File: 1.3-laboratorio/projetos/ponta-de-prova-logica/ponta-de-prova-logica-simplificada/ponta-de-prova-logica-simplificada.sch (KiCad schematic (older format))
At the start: 18 parts, among them J1 TEST PROBE, J2 Conn_01x02, U1 LM319

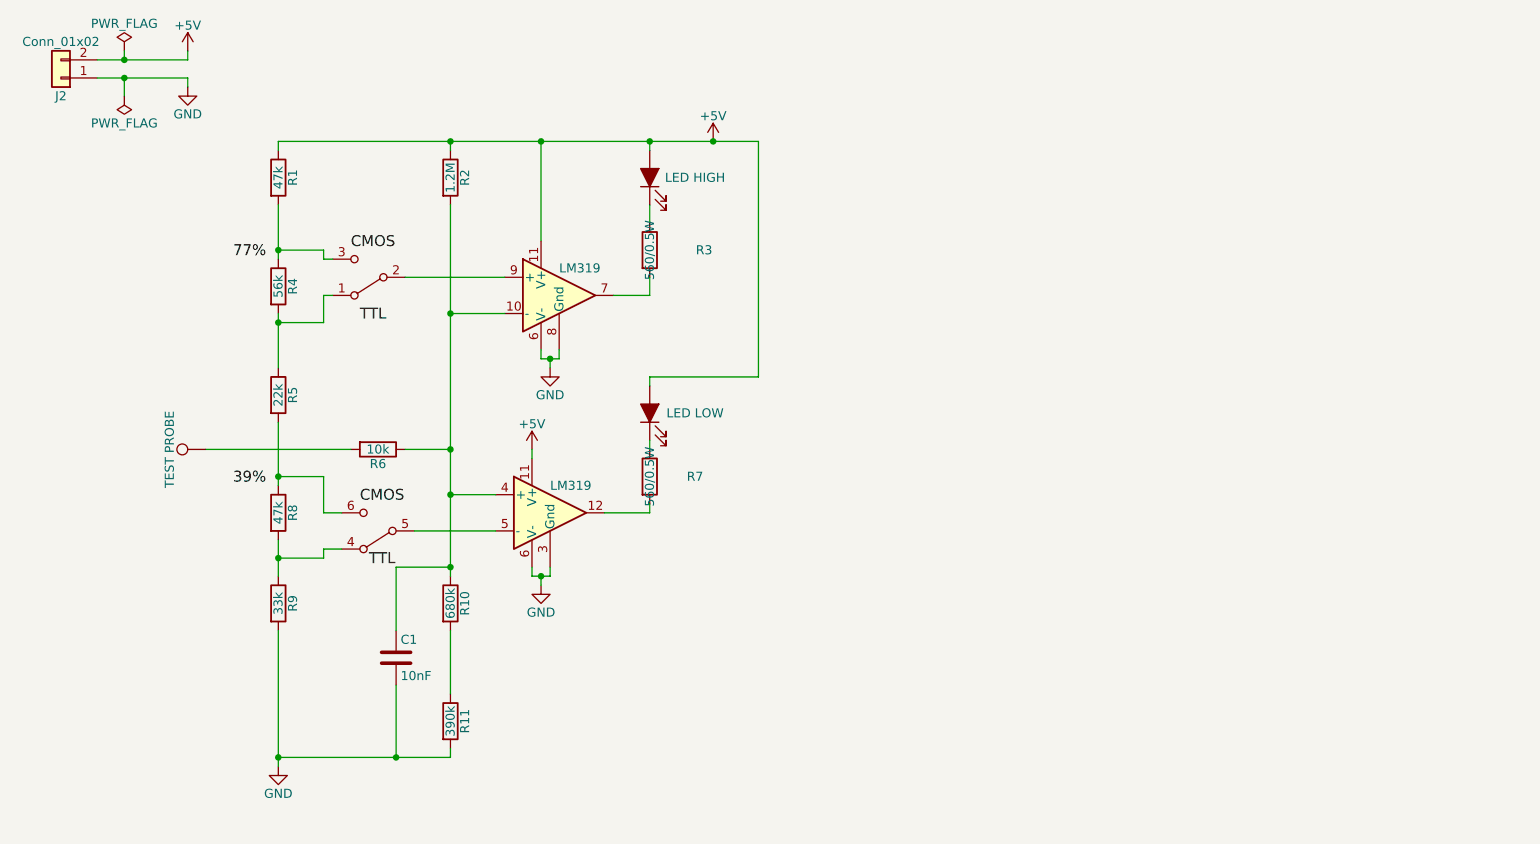
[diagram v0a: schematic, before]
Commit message: Nova versão da Ponta de Prova Lógica com o LM339.
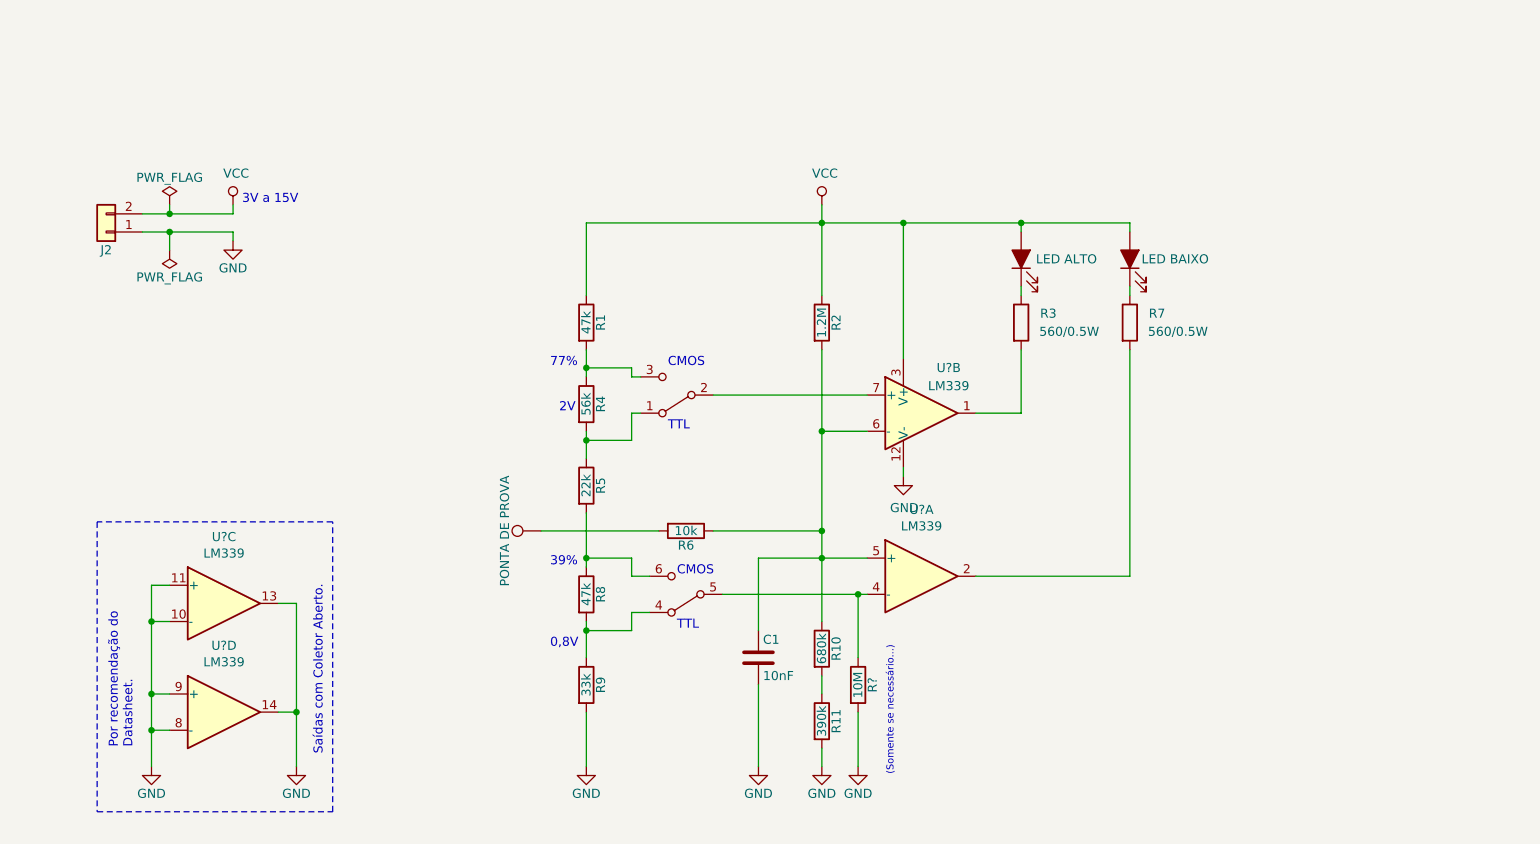
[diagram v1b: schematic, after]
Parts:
- removed U1: LM319, Housings_DIP:DIP-14_W7.62mm, symbol ponta-de-prova-logica-simplificada-rescue:LM319
- added R?: 10M, Resistors_THT:R_Axial_DIN0207_L6.3mm_D2.5mm_P7.62mm_Horizontal, symbol Device:R
- added U? (x5): LM339, symbol Comparator:LM339
- D1: value LED HIGH -> LED ALTO
- D2: value LED LOW -> LED BAIXO
- J1: value TEST PROBE -> PONTA DE PROVA
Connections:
- net GND: now also R?.2, U?.10 (-), U?.11 (+), U?.12 (V-), U?.13, U?.14, U?.8 (-), U?.9 (+)
- net at C1.1, R10.1, R2.2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: now also U?.5 (+), U?.6 (-)
- net at R3.2: now also U?.1
- net at TTL1.2 (B): now also U?.7 (+)
- net at R7.2: now also U?.2
- net at TTL1.5 (B): now also R?.1, U?.4 (-)
- net +5V renamed VCC
- net VCC: now also U?.3 (V+)
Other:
- note added: "(Somente se necessário...)"
- note added: "0,8V"
- note added: "2V"
- note added: "39%"
- note added: "3V a 15V"
- note added: "77%"
- note added: "CMOS"
- note added: "Por recomendação do\nDatasheet."
- note added: "Saídas com Coletor Aberto."
- note added: "TTL"
- moved on the sheet: C1, J2, R1, R10, R11, R2, R3, R4, R5, R6, R7, R8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

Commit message: Nova versão da Ponta de Prova Lógica - PCI em elaboração.
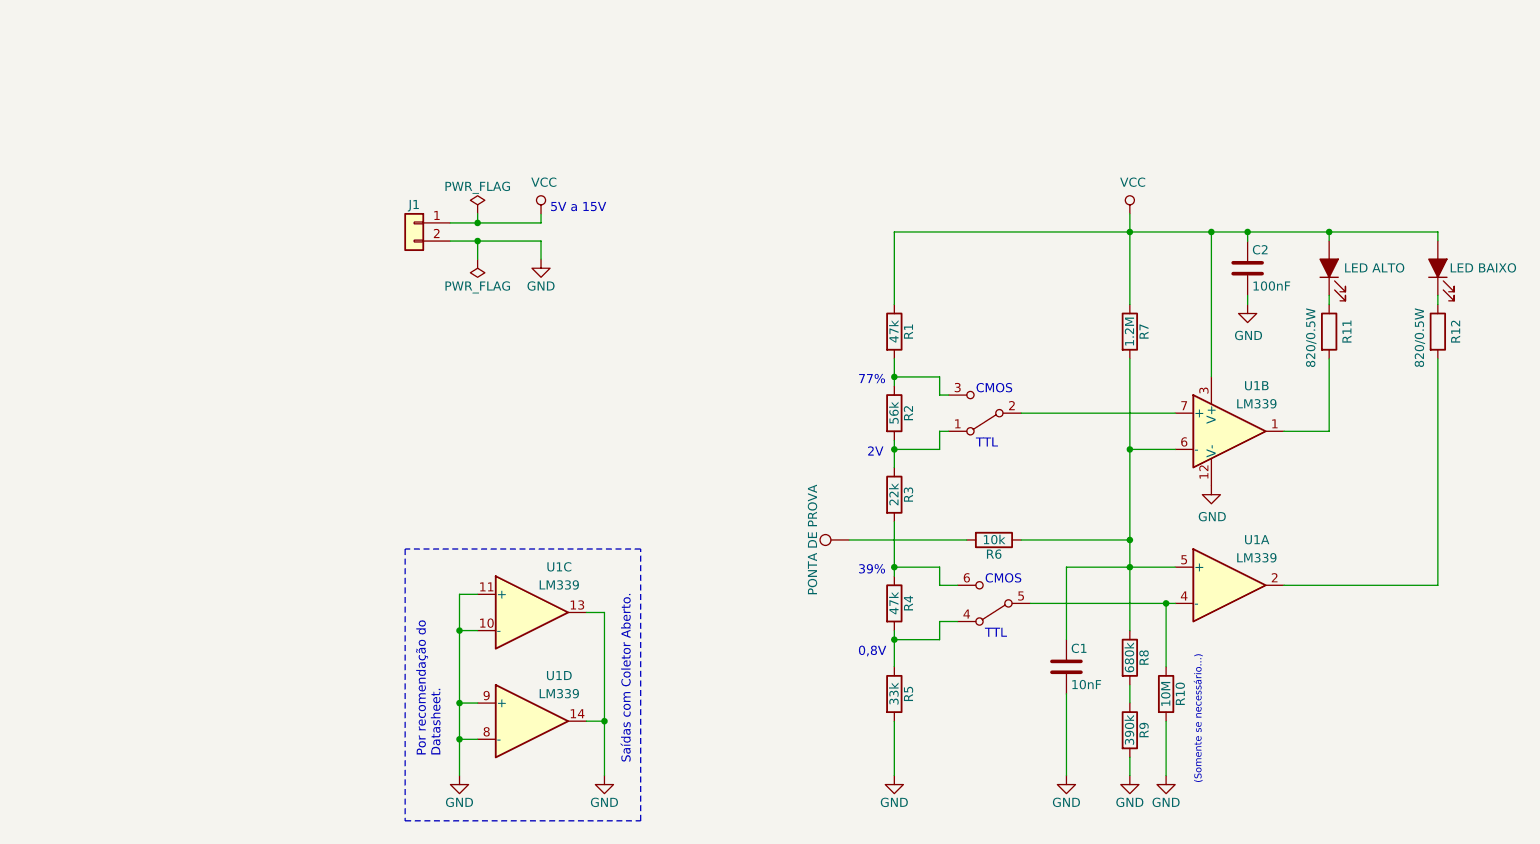
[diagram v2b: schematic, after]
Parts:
- added C2: 100nF, Capacitor_THT:C_Disc_D5.0mm_W2.5mm_P5.00mm, symbol Device:C
- C1: footprint Capacitors_THT:C_Disc_D5.0mm_W2.5mm_P5.00mm -> Capacitor_THT:C_Disc_D5.0mm_W2.5mm_P5.00mm
- D1, D2: footprint LEDs:LED_D4.0mm -> LED_THT:LED_D3.0mm
- J1: renamed from J2; footprint Connectors_Terminal_Blocks:TerminalBlock_Altech_AK300-2_P5.00mm -> TerminalBlock:TerminalBlock_Altech_AK300-2_P5.00mm
- J2: renamed from J1; footprint Connectors:Pin_d1.0mm_L10.0mm -> Connector_Wire:SolderWirePad_1x01_Drill0.8mm
- R1, R6: footprint Resistors_THT:R_Axial_DIN0207_L6.3mm_D2.5mm_P7.62mm_Horizontal -> Resistor_THT:R_Axial_DIN0207_L6.3mm_D2.5mm_P7.62mm_Horizontal
- R10: renamed from R?; footprint Resistors_THT:R_Axial_DIN0207_L6.3mm_D2.5mm_P7.62mm_Horizontal -> Resistor_THT:R_Axial_DIN0207_L6.3mm_D2.5mm_P7.62mm_Horizontal
- R11: renamed from R3; value 560/0.5W -> 820/0.5W; footprint Resistors_THT:R_Axial_DIN0207_L6.3mm_D2.5mm_P7.62mm_Horizontal -> Resistor_THT:R_Axial_DIN0207_L6.3mm_D2.5mm_P7.62mm_Horizontal
- R12: renamed from R7; value 560/0.5W -> 820/0.5W; footprint Resistors_THT:R_Axial_DIN0207_L6.3mm_D2.5mm_P7.62mm_Horizontal -> Resistor_THT:R_Axial_DIN0207_L6.3mm_D2.5mm_P7.62mm_Horizontal
- R2: renamed from R4; footprint Resistors_THT:R_Axial_DIN0207_L6.3mm_D2.5mm_P7.62mm_Horizontal -> Resistor_THT:R_Axial_DIN0207_L6.3mm_D2.5mm_P7.62mm_Horizontal
- R3: renamed from R5; footprint Resistors_THT:R_Axial_DIN0207_L6.3mm_D2.5mm_P7.62mm_Horizontal -> Resistor_THT:R_Axial_DIN0207_L6.3mm_D2.5mm_P7.62mm_Horizontal
- R4: renamed from R8; footprint Resistors_THT:R_Axial_DIN0207_L6.3mm_D2.5mm_P7.62mm_Horizontal -> Resistor_THT:R_Axial_DIN0207_L6.3mm_D2.5mm_P7.62mm_Horizontal
- R5: renamed from R9; footprint Resistors_THT:R_Axial_DIN0207_L6.3mm_D2.5mm_P7.62mm_Horizontal -> Resistor_THT:R_Axial_DIN0207_L6.3mm_D2.5mm_P7.62mm_Horizontal
- R7: renamed from R2; footprint Resistors_THT:R_Axial_DIN0207_L6.3mm_D2.5mm_P7.62mm_Horizontal -> Resistor_THT:R_Axial_DIN0207_L6.3mm_D2.5mm_P7.62mm_Horizontal
- R8: renamed from R10; footprint Resistors_THT:R_Axial_DIN0207_L6.3mm_D2.5mm_P7.62mm_Horizontal -> Resistor_THT:R_Axial_DIN0207_L6.3mm_D2.5mm_P7.62mm_Horizontal
- R9: renamed from R11; footprint Resistors_THT:R_Axial_DIN0207_L6.3mm_D2.5mm_P7.62mm_Horizontal -> Resistor_THT:R_Axial_DIN0207_L6.3mm_D2.5mm_P7.62mm_Horizontal
- TTL1: footprint Buttons_Switches_THT:SW_CuK_JS202011AQN_DPDT_Angled -> Button_Switch_THT:SW_CuK_JS202011CQN_DPDT_Straight
- U1: renamed from U?; footprint (none) -> Package_DIP:DIP-14_W7.62mm_Socket_LongPads
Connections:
- net GND: now also J1.2 (Pin_2), C2.2; no longer J1.1 (Pin_1)
- net VCC: now also J1.1 (Pin_1), C2.1; no longer J1.2 (Pin_2)
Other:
- note added: "5V a 15V"
- note removed: "3V a 15V"
- moved on the sheet: C1, J1, R1, R10, R11, R12, R2, R3, R4, R5, R6, R7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

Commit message: Gerbers e sincronização.
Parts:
- SW1: renamed from TTL1; footprint Button_Switch_THT:SW_CuK_JS202011CQN_DPDT_Straight -> Buttons_Switches_ThroughHole:SW_CuK_JS202011CQN_DPDT_Straight
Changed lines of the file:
@@
 Connection ~ 8100 2250
 $Comp
-L ponta-de-prova-logica-simplificada-rescue:SW_DPDT_x2 TTL1
+L ponta-de-prova-logica-simplificada-rescue:SW_DPDT_x2 SW1
 U 2 1 5BBF4AF5
 P 6250 4300
-F 0 "TTL1" H 6250 4470 50  0001 C CNN
+F 0 "SW1" H 6000 4250 50  0000 C CNN
 F 1 "SW_DPDT_x2" H 6250 4100 50  0001 C CNN
-F 2 "Button_Switch_THT:SW_CuK_JS202011CQN_DPDT_Straight" H 6250 4300 50  0001 C CNN
+F 2 "Buttons_Switches_ThroughHole:SW_CuK_JS202011CQN_DPDT_Straight" H 6250 4300 50  0001 C CNN
 F 3 "" H 6250 4300 50  0001 C CNN
 	2    6250 4300
@@
 Connection ~ 5700 4100
 $Comp
-L ponta-de-prova-logica-simplificada-rescue:SW_DPDT_x2 TTL1
+L ponta-de-prova-logica-simplificada-rescue:SW_DPDT_x2 SW1
 U 1 1 5BBF503E
 P 6200 3250
-F 0 "TTL1" H 6200 3420 50  0001 C CNN
+F 0 "SW1" H 5950 3200 50  0000 C CNN
 F 1 "SW_DPDT_x2" H 6200 3050 50  0001 C CNN
-F 2 "Button_Switch_THT:SW_CuK_JS202011CQN_DPDT_Straight" H 6200 3250 50  0001 C CNN
+F 2 "Buttons_Switches_ThroughHole:SW_CuK_JS202011CQN_DPDT_Straight" H 6200 3250 50  0001 C CNN
 F 3 "" H 6200 3250 50  0001 C CNN
 	1    6200 3250
